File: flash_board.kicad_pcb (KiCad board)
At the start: 2 copper layers, 55.4 x 45.7 mm, 9 parts, among them J1 Conn_02x16_Row_Letter_First, J2 Conn_02x03_Counter_Clockwise, U1 SST39SF040

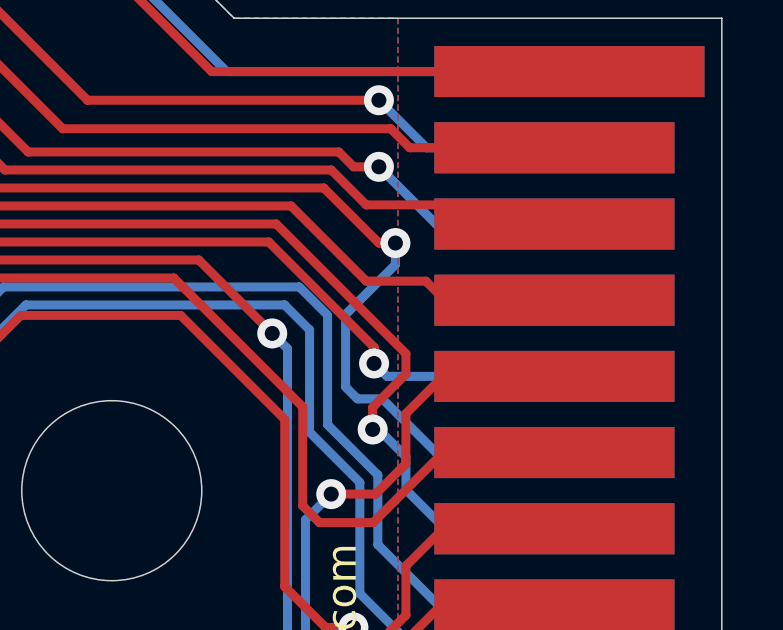
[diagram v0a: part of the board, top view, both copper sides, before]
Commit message: Fixed D5 location on connector.
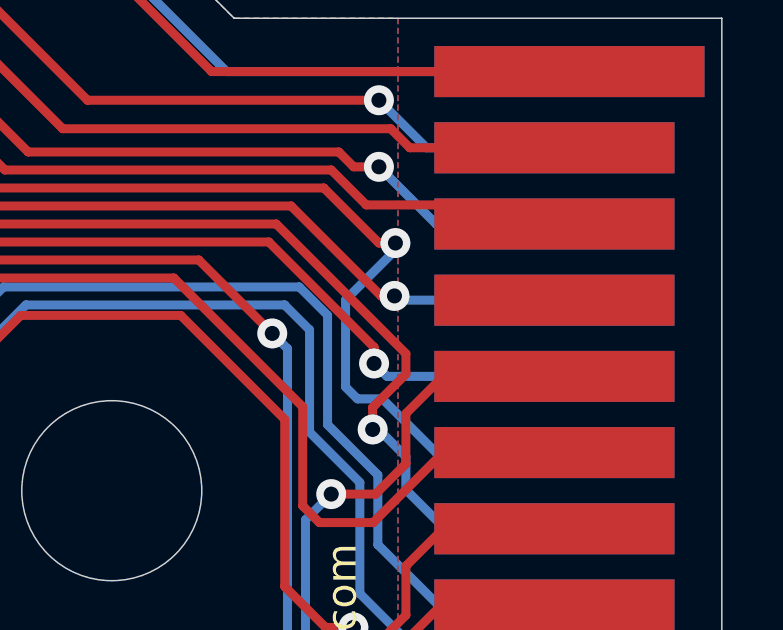
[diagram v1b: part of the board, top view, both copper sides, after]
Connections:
- J1 pad a4: unconnected-(J1-Pin_a4-Pada4) -> /D5
- J1 pad b4: /D5 -> unconnected-(J1-Pin_b4-Padb4)
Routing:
- net unconnected-(J1-Pin_b4-Padb4): track 0.00 -> 4.15 mm
- net /D5: track 40.8 -> 40.3 mm, vias 0 -> 1
